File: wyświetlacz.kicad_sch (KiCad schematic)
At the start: 0 parts

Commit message: Pinout dla ESP32
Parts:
- added U5: ER_OLEDM0.91_1x-I2C, Display:ER_OLEDM0.91_1x-I2C, symbol Display_Graphic:ER_OLEDM0.91_1x-I2C
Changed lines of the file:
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@@
 	(generator_version "10.0")
 	(paper "A4")
+	(symbol
+		(lib_id "Display_Graphic:ER_OLEDM0.91_1x-I2C")
+		(at 135.89 86.36 0)
+		(unit 1)
+		(body_style 1)
+		(exclude_from_sim no)
+		(in_bom yes)
+		(on_board yes)
+		(in_pos_files yes)
+		(dnp no)
+		(fields_autoplaced yes)
+		(property "Reference" "U5"
+			(at 144.78 85.0899 0)
+			(show_name no)
+			(do_not_autoplace no)
+			(effects
+				(font
+					(size 1.27 1.27)
+				)
+				(justify left)
+			)
+		)
+		(property "Value" "ER_OLEDM0.91_1x-I2C"
+			(at 144.78 87.6299 0)
+			(show_name no)
+			(do_not_autoplace no)
+			(effects
+				(font
+					(size 1.27 1.27)
+				)
+				(justify left)
+			)
+		)
+		(property "Footprint" "Display:ER_OLEDM0.91_1x-I2C"
+			(at 153.924 99.06 0)
+			(hide yes)
+			(show_name no)
+			(do_not_autoplace no)
+			(effects
+				(font
+					(size 1.27 1.27)
+				)
+			)
+		)
+		(property "Datasheet" "https://www.buydisplay.com/download/manual/ER-OLEDM0.91-1_Datasheet.pdf"
+			(at 178.562 101.092 0)
+			(hide yes)
+			(show_name no)
+			(do_not_autoplace no)
+			(effects
+				(font
+					(size 1.27 1.27)
+				)
+			)
+		)
+		(property "Description" "SSD1306 OLED module, 0.91 inch, 128x32, I2C"
+			(at 162.56 103.124 0)
+			(hide yes)
+			(show_name no)
+			(do_not_autoplace no)
+			(effects
+				(font
+					(size 1.27 1.27)
+				)
+			)
+		)
+		(pin "2"
+		)
+		(pin "1"
+		)
+		(pin "4"
+		)
+		(pin "3"
+		)
+		(instances
+			(project "Projekt_smiw"
+				(path "/d5cd91f9-1e43-4778-a798-2ad13ae8c439"
+					(reference "U5")
+					(unit 1)
+				)
+			)
+		)
+	)
 	(sheet_instances
 		(path "/"

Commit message: wyswietlacz 1
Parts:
- added C10: 100nF, symbol Device:C_Small
- added J7: Conn_W, symbol Connector_Generic:Conn_02x02_Counter_Clockwise
- added R10, R11, R12, R7: 10k, symbol Device:R_Small
- added U4: MB85RC256V, Package_SO:SOIC-8_3.9x4.9mm_P1.27mm, symbol Memory_NVRAM:FM24C64B
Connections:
- net GND: now reaches U5.1 (GND)
- net GND: now also C10.1, J7.3 (Pin_3), R11.2, R12.2, R7.2, U4.4 (VSS)
- net VDD3: now reaches U5.2 (VCC)
- net VDD3: now also C10.2, J7.1 (Pin_1), R10.1, U4.8 (VDD)
- net SCL: now reaches U5.3 (SCL)
- net SCL: now also J7.4 (Pin_4), U4.6 (SCL)
- net SDA: now reaches U5.4 (SDA)
- net SDA: now also J7.2 (Pin_2), U4.5 (SDA)
- new net: R12.1, U4.1 (A0)
- new net: R10.2, U4.7 (WP)
- new net: R11.1, U4.2 (A1)
- new net: R7.1, U4.3 (A2)
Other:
- moved on the sheet: U5

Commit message: Orange 21.37
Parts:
- removed J7: Conn_W, symbol Connector_Generic:Conn_02x02_Counter_Clockwise
- added J5: Conn, symbol Connector_Generic:Conn_02x09_Odd_Even
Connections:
- net GND: now also R10.2, J5.17 (Pin_17), J5.18 (Pin_18)
- net SCL: now also J5.15 (Pin_15)
- net SDA: now also J5.13 (Pin_13)
- net VDD3: now also J5.1 (Pin_1); no longer R10.1
- net at U4.7 (WP): now also R10.1; no longer R10.2

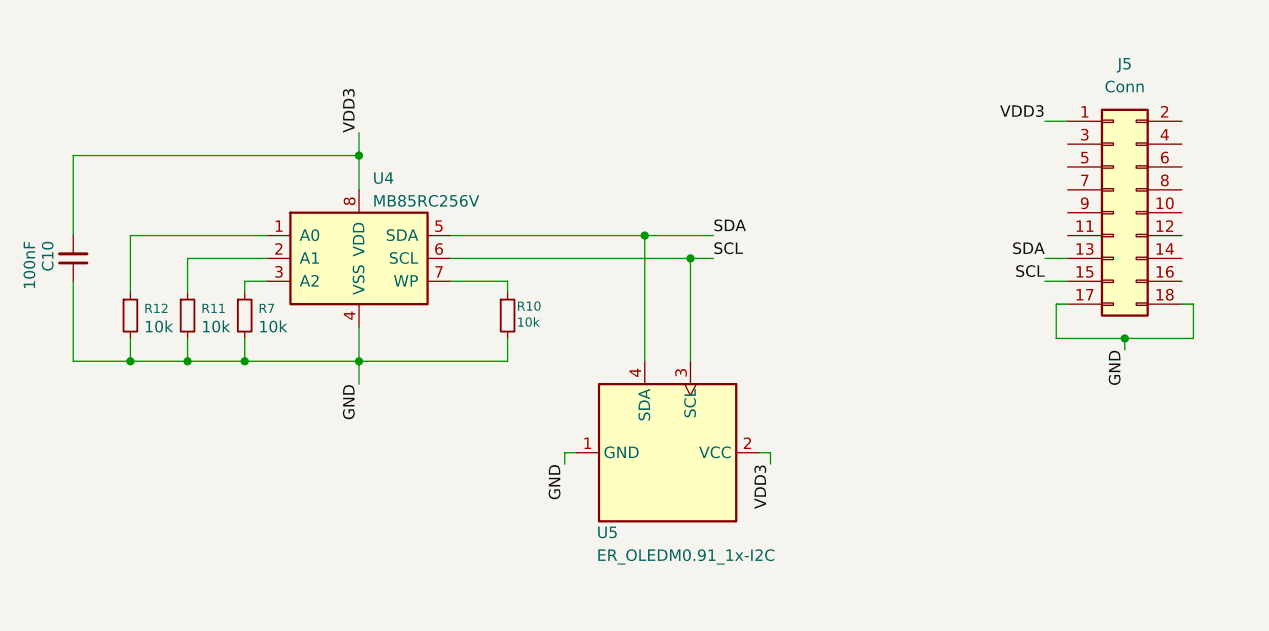
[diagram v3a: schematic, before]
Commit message: USB C update
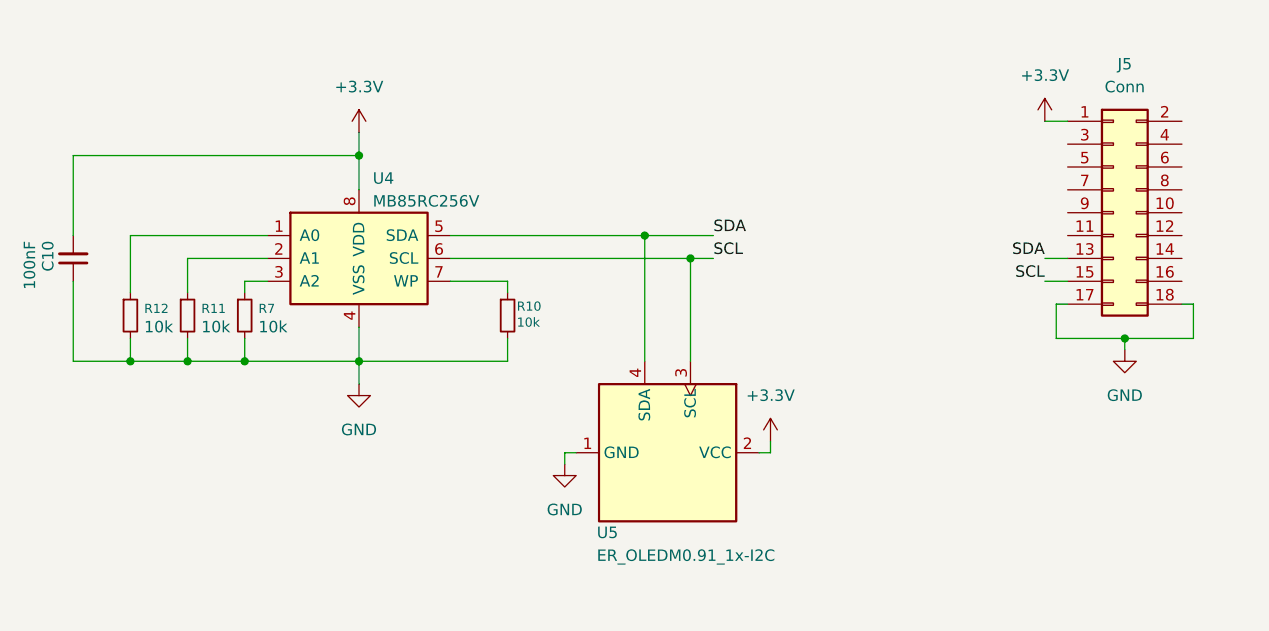
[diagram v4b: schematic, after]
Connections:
- net VDD3 renamed +3.3V

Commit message: małe zmiany poprawki dsagolih
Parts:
- renumbered R11 to R10, R7 to R11, R10 to R12, R12 to R9, U4 to U6, U5 to U7
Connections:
- no-connect marks 0 -> 13
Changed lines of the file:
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@@
 		(color 0 0 0 0)
 	)
+	(no_connect
+		(at 224.79 41.91)
+	)
+	(no_connect
+		(at 224.79 52.07)
+	)
+	(no_connect
+		(at 209.55 54.61)
+	)
+	(no_connect
+		(at 224.79 57.15)
+	)
+	(no_connect
+		(at 224.79 46.99)
+	)
+	(no_connect
+		(at 209.55 52.07)
+	)
+	(no_connect
+		(at 224.79 54.61)
+	)
+	(no_connect
+		(at 224.79 59.69)
+	)
+	(no_connect
+		(at 209.55 49.53)
+	)
+	(no_connect
+		(at 209.55 46.99)
+	)
+	(no_connect
+		(at 224.79 44.45)
+	)
+	(no_connect
+		(at 224.79 49.53)
+	)
+	(no_connect
+		(at 209.55 44.45)
+	)
 	(wire
 		(pts
@@
 	(wire
 		(pts
+			(xy 224.79 41.91) (xy 223.52 41.91)
+		)
+		(stroke
+			(width 0)
+			(type default)
+		)
+	)
+	(wire
+		(pts
 			(xy 176.53 78.74) (xy 177.8 78.74)
 		)
@@
 	(wire
 		(pts
+			(xy 224.79 52.07) (xy 223.52 52.07)
+		)
+		(stroke
+			(width 0)
+			(type default)
+		)
+	)
+	(wire
+		(pts
 			(xy 148.59 68.58) (xy 132.08 68.58)
 		)
@@
 	(wire
 		(pts
+			(xy 224.79 49.53) (xy 223.52 49.53)
+		)
+		(stroke
+			(width 0)
+			(type default)
+		)
+	)
+	(wire
+		(pts
 			(xy 132.08 68.58) (xy 132.08 64.77)
 		)
@@
 	(wire
 		(pts
+			(xy 224.79 59.69) (xy 223.52 59.69)
+		)
+		(stroke
+			(width 0)
+			(type default)
+		)
+	)
+	(wire
+		(pts
 			(xy 113.03 68.58) (xy 106.68 68.58)
 		)
@@
 	(wire
 		(pts
+			(xy 224.79 54.61) (xy 223.52 54.61)
+		)
+		(stroke
+			(width 0)
+			(type default)
+		)
+	)
+	(wire
+		(pts
 			(xy 132.08 43.18) (xy 132.08 45.72)
 		)
@@
 	(wire
 		(pts
+			(xy 209.55 44.45) (xy 210.82 44.45)
+		)
+		(stroke
+			(width 0)
+			(type default)
+		)
+	)
+	(wire
+		(pts
 			(xy 148.59 59.69) (xy 148.59 60.96)
 		)
@@
 	(wire
 		(pts
+			(xy 224.79 46.99) (xy 223.52 46.99)
+		)
+		(stroke
+			(width 0)
+			(type default)
+		)
+	)
+	(wire
+		(pts
 			(xy 163.83 54.61) (xy 163.83 68.58)
 		)
@@
 	(wire
 		(pts
+			(xy 209.55 49.53) (xy 210.82 49.53)
+		)
+		(stroke
+			(width 0)
+			(type default)
+		)
+	)
+	(wire
+		(pts
 			(xy 113.03 60.96) (xy 113.03 57.15)
 		)
@@
 	(wire
 		(pts
+			(xy 209.55 52.07) (xy 210.82 52.07)
+		)
+		(stroke
+			(width 0)
+			(type default)
+		)
+	)
+	(wire
+		(pts
+			(xy 224.79 57.15) (xy 223.52 57.15)
+		)
+		(stroke
+			(width 0)
+			(type default)
+		)
+	)
+	(wire
+		(pts
 			(xy 209.55 66.04) (xy 209.55 62.23)
 		)
@@
 	(wire
 		(pts
+			(xy 209.55 46.99) (xy 210.82 46.99)
+		)
+		(stroke
+			(width 0)
+			(type default)
+		)
+	)
+	(wire
+		(pts
 			(xy 208.28 59.69) (xy 210.82 59.69)
 		)
@@
 		(pts
 			(xy 224.79 66.04) (xy 224.79 62.23)
+		)
+		(stroke
+			(width 0)
+			(type default)
+		)
+	)
+	(wire
+		(pts
+			(xy 209.55 54.61) (xy 210.82 54.61)
+		)
+		(stroke
+			(width 0)
+			(type default)
+		)
+	)
+	(wire
+		(pts
+			(xy 224.79 44.45) (xy 223.52 44.45)
 		)
 		(stroke
@@
 		(dnp no)
 		(fields_autoplaced yes)
-		(property "Reference" "#PWR028"
+		(property "Reference" "#PWR029"
 			(at 177.8 81.28 0)
 			(hide yes)
@@
 			(project "Projekt_smiw"
 				(path "/d5cd91f9-1e43-4778-a798-2ad13ae8c439"
-					(reference "#PWR028")
+					(reference "#PWR029")
 					(unit 1)
 				)
@@
 		(in_pos_files yes)
 		(dnp no)
-		(property "Reference" "R12"
+		(property "Reference" "R9"
 			(at 108.204 62.738 0)
 			(show_name no)
@@
 			(project "Projekt_smiw"
 				(path "/d5cd91f9-1e43-4778-a798-2ad13ae8c439"
-					(reference "R12")
+					(reference "R9")
 					(unit 1)
 				)
@@
 		(in_pos_files yes)
 		(dnp no)
-		(property "Reference" "U5"
+		(property "Reference" "U7"
 			(at 158.496 87.63 90)
 			(show_name no)
@@
 			(project "Projekt_smiw"
 				(path "/d5cd91f9-1e43-4778-a798-2ad13ae8c439"
-					(reference "U5")
+					(reference "U7")
 					(unit 1)
 				)
@@
 		(dnp no)
 		(fields_autoplaced yes)
-		(property "Reference" "#PWR029"
+		(property "Reference" "#PWR026"
 			(at 132.08 46.99 0)
 			(hide yes)
@@
 			(project "Projekt_smiw"
 				(path "/d5cd91f9-1e43-4778-a798-2ad13ae8c439"
-					(reference "#PWR029")
+					(reference "#PWR026")
 					(unit 1)
 				)
@@
 		(dnp no)
 		(fields_autoplaced yes)
-		(property "Reference" "#PWR015"
+		(property "Reference" "#PWR028"
 			(at 154.94 86.36 0)
 			(hide yes)
@@
 			(project "Projekt_smiw"
 				(path "/d5cd91f9-1e43-4778-a798-2ad13ae8c439"
-					(reference "#PWR015")
+					(reference "#PWR028")
 					(unit 1)
 				)
@@
 		(in_pos_files yes)
 		(dnp no)
-		(property "Reference" "R11"
+		(property "Reference" "R10"
 			(at 114.554 62.738 0)
 			(show_name no)
@@
 			(project "Projekt_smiw"
 				(path "/d5cd91f9-1e43-4778-a798-2ad13ae8c439"
-					(reference "R11")
+					(reference "R10")
 					(unit 1)
 				)
@@
 		(dnp no)
 		(fields_autoplaced yes)
-		(property "Reference" "#PWR027"
+		(property "Reference" "#PWR030"
 			(at 208.28 45.72 0)
 			(hide yes)
@@
 			(project "Projekt_smiw"
 				(path "/d5cd91f9-1e43-4778-a798-2ad13ae8c439"
-					(reference "#PWR027")
+					(reference "#PWR030")
 					(unit 1)
 				)
@@
 		(in_pos_files yes)
 		(dnp no)
-		(property "Reference" "R7"
+		(property "Reference" "R11"
 			(at 120.904 62.738 0)
 			(show_name no)
@@
 			(project "Projekt_smiw"
 				(path "/d5cd91f9-1e43-4778-a798-2ad13ae8c439"
-					(reference "R7")
+					(reference "R11")
 					(unit 1)
 				)
@@
 		(dnp no)
 		(fields_autoplaced yes)
-		(property "Reference" "#PWR012"
+		(property "Reference" "#PWR031"
 			(at 217.17 73.66 0)
 			(hide yes)
@@
 			(project "Projekt_smiw"
 				(path "/d5cd91f9-1e43-4778-a798-2ad13ae8c439"
-					(reference "#PWR012")
+					(reference "#PWR031")
 					(unit 1)
 				)
@@
 		(in_pos_files yes)
 		(dnp no)
-		(property "Reference" "U4"
+		(property "Reference" "U6"
 			(at 133.604 48.26 0)
 			(show_name no)
@@
 			(project "Projekt_smiw"
 				(path "/d5cd91f9-1e43-4778-a798-2ad13ae8c439"
-					(reference "U4")
+					(reference "U6")
 					(unit 1)
 				)
@@
 		(dnp no)
 		(fields_autoplaced yes)
-		(property "Reference" "#PWR026"
+		(property "Reference" "#PWR027"
 			(at 132.08 77.47 0)
 			(hide yes)
@@
 			(project "Projekt_smiw"
 				(path "/d5cd91f9-1e43-4778-a798-2ad13ae8c439"
-					(reference "#PWR026")
+					(reference "#PWR027")
 					(unit 1)
 				)
@@
 		(in_pos_files yes)
 		(dnp no)
-		(property "Reference" "R10"
+		(property "Reference" "R12"
 			(at 149.606 62.484 0)
 			(show_name no)
@@
 			(project "Projekt_smiw"
 				(path "/d5cd91f9-1e43-4778-a798-2ad13ae8c439"
-					(reference "R10")
+					(reference "R12")
 					(unit 1)
 				)

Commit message: footprinty all, aheoi;rthipoawert;hiogsedho;i yay Halo? Schemat zrobiony ^^ pewnie nie
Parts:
- removed J5: Conn, symbol Connector_Generic:Conn_02x09_Odd_Even
- added J8: Conn IN, Connector_PinHeader_2.54mm:PinHeader_2x09_P2.54mm_Vertical, symbol Connector_Generic:Conn_02x09_Odd_Even
- C15: renamed from C10; footprint (none) -> Capacitor_SMD:C_0603_1608Metric
- R10: renamed from R11; footprint (none) -> Resistor_SMD:R_0603_1608Metric
- R11: renamed from R12; footprint (none) -> Resistor_SMD:R_0603_1608Metric
- R8: renamed from R9; footprint (none) -> Resistor_SMD:R_0603_1608Metric
- R9: renamed from R10; footprint (none) -> Resistor_SMD:R_0603_1608Metric
- U7: value ER_OLEDM0.91_1x-I2C -> SSD1306
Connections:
- net +3.3V: now also J8.1 (Pin_1)
- net GND: now also J8.17 (Pin_17), J8.18 (Pin_18)
- net SCL: now also J8.15 (Pin_15)
- net SDA: now also J8.13 (Pin_13)
- new net COL 1: J8.2 (Pin_2)
- new net COL 2: J8.4 (Pin_4)
- new net COL 3: J8.6 (Pin_6)
- new net COL 4: J8.8 (Pin_8)
- new net CS BME280: J8.3 (Pin_3)
- new net CS FRAM SPI: J8.5 (Pin_5)
- new net MISO: J8.9 (Pin_9)
- new net MOSI: J8.7 (Pin_7)
- new net ROW 1: J8.10 (Pin_10)
- new net ROW 2: J8.12 (Pin_12)
- new net ROW 3: J8.14 (Pin_14)
- new net ROW 4: J8.16 (Pin_16)
- new net SCK: J8.11 (Pin_11)
- no-connect marks 13 -> 0

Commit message: awetg
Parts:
- removed J8: Conn IN, Connector_PinHeader_2.54mm:PinHeader_2x09_P2.54mm_Vertical, symbol Connector_Generic:Conn_02x09_Odd_Even
- added J8: Conn_01x08, Connector_PinHeader_2.54mm:PinHeader_1x08_P2.54mm_Vertical, symbol Connector_Generic:Conn_01x08
- added J9: Conn_01x10, Connector_PinHeader_2.54mm:PinHeader_1x10_P2.54mm_Vertical, symbol Connector_Generic:Conn_01x10
- renumbered U6 to U7, U7 to U8
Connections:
- net +3.3V: now also J8.1 (Pin_1)
- net COL 1: now also J9.1 (Pin_1)
- net COL 2: now also J9.2 (Pin_2)
- net COL 3: now also J9.3 (Pin_3)
- net COL 4: now also J9.4 (Pin_4)
- net CS BME280: now also J8.2 (Pin_2)
- net CS FRAM SPI: now also J8.3 (Pin_3)
- net GND: now also J9.10 (Pin_10), J9.9 (Pin_9)
- net MISO: now also J8.5 (Pin_5)
- net MOSI: now also J8.4 (Pin_4)
- net ROW 1: now also J9.5 (Pin_5)
- net ROW 2: now also J9.6 (Pin_6)
- net ROW 3: now also J9.7 (Pin_7)
- net ROW 4: now also J9.8 (Pin_8)
- net SCK: now also J8.6 (Pin_6)
- net SCL: now also J8.8 (Pin_8)
- net SDA: now also J8.7 (Pin_7)
